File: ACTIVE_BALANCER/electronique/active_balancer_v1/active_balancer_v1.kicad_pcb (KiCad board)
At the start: 2 copper layers, 1 part, among them U1 LTC3300ILXE-2_PBF

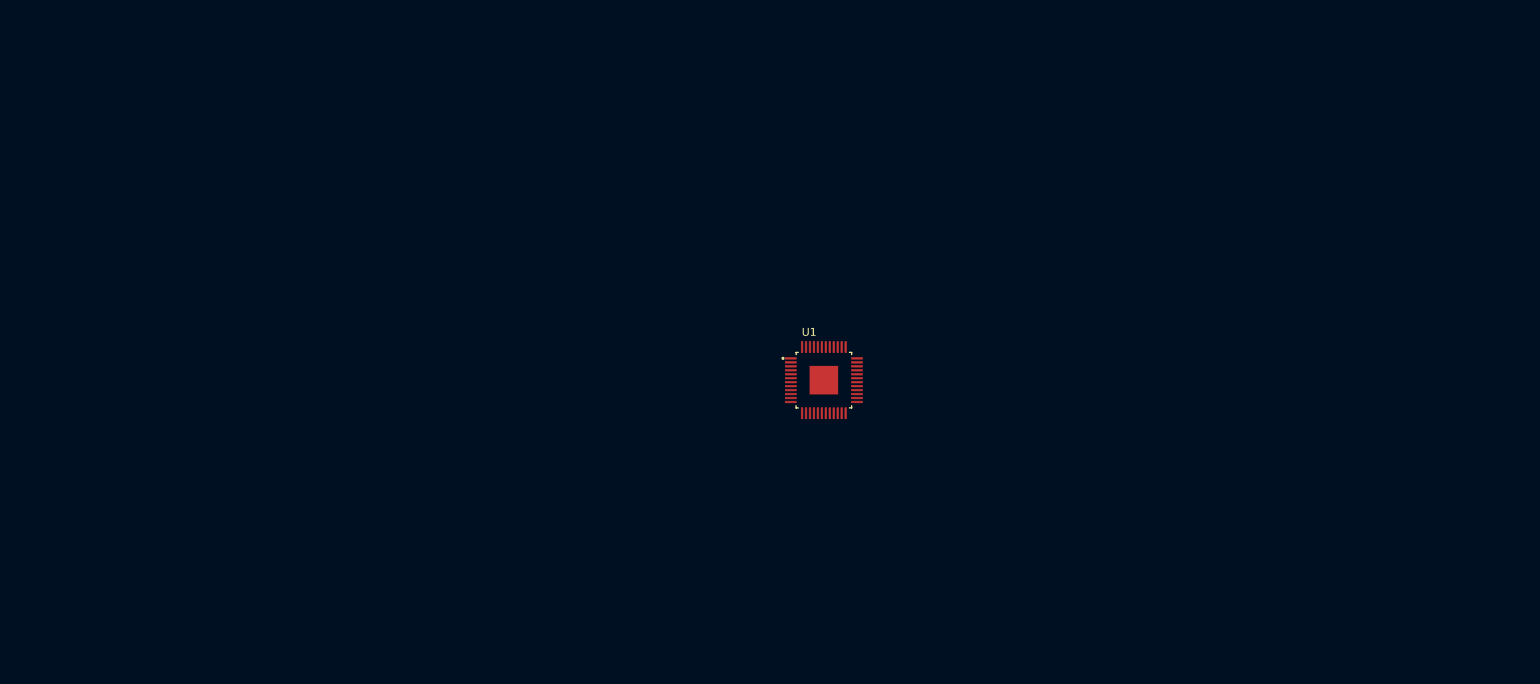
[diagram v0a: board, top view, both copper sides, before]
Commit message: finished the schematic need a review to make shure everything is okay and after pcb placing & routing while be made. Note this active balancer is for 6s scallable easly for 64s
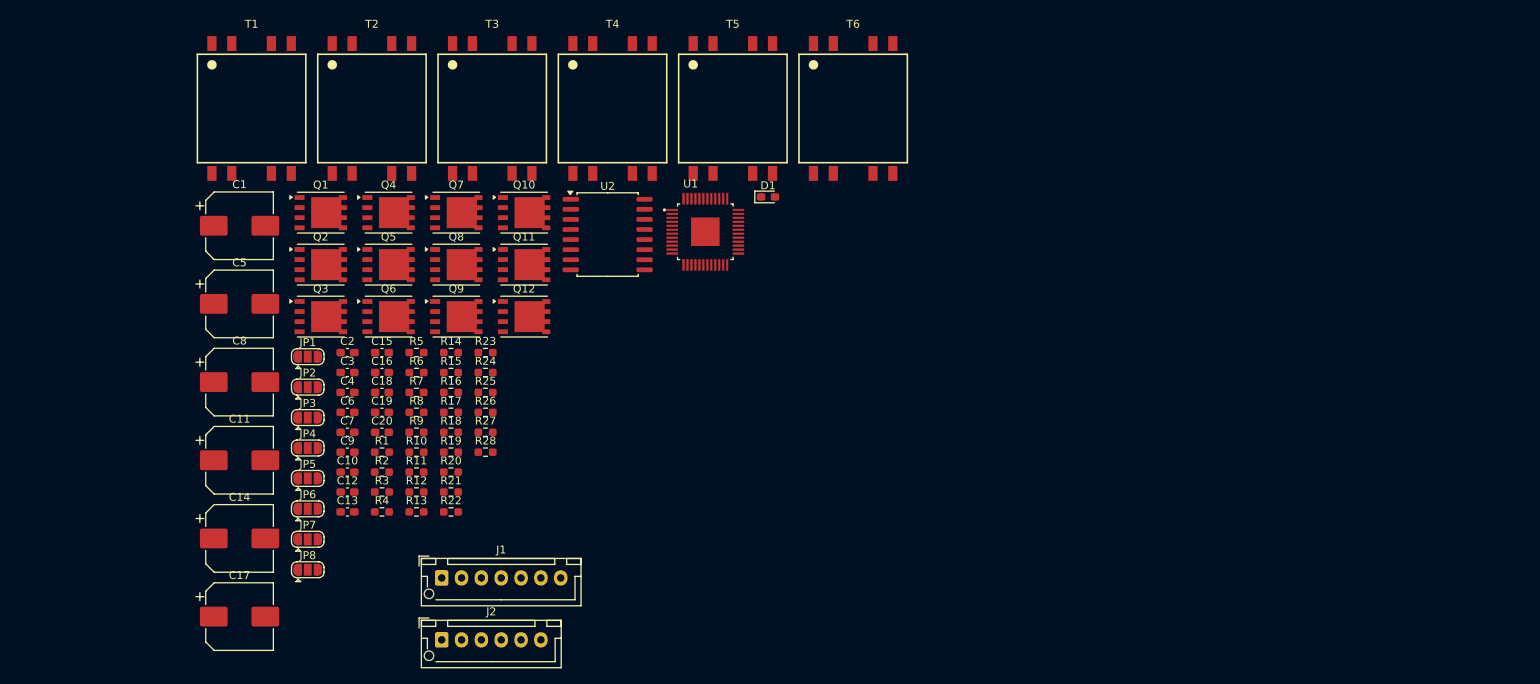
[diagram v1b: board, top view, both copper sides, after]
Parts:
- added C1: 60uF 10V, Capacitor_SMD:CP_Elec_8x10, F.Cu at (84.7, 70.7)
- added C10: 100pF 100V, Capacitor_SMD:C_0603_1608Metric_Pad1.08x0.95mm_HandSolder, F.Cu at (98.3, 101.7)
- added C11: 60uF 10V, Capacitor_SMD:CP_Elec_8x10, F.Cu at (84.7, 100.2)
- added C12: 100pF 100V, Capacitor_SMD:C_0603_1608Metric_Pad1.08x0.95mm_HandSolder, F.Cu at (98.3, 104.2)
- added C13: 100pF 100V, Capacitor_SMD:C_0603_1608Metric_Pad1.08x0.95mm_HandSolder, F.Cu at (98.3, 106.7)
- added C14: 60uF 10V, Capacitor_SMD:CP_Elec_8x10, F.Cu at (84.7, 110.1)
- added C15: 100pF 100V, Capacitor_SMD:C_0603_1608Metric_Pad1.08x0.95mm_HandSolder, F.Cu at (102.6, 86.6)
- added C16: 100pF 100V, Capacitor_SMD:C_0603_1608Metric_Pad1.08x0.95mm_HandSolder, F.Cu at (102.6, 89.1)
- added C17: 60uF 10V, Capacitor_SMD:CP_Elec_8x10, F.Cu at (84.7, 119.9)
- added C18: 100pF 100V, Capacitor_SMD:C_0603_1608Metric_Pad1.08x0.95mm_HandSolder, F.Cu at (102.6, 91.7)
- added C19: 100pF 100V, Capacitor_SMD:C_0603_1608Metric_Pad1.08x0.95mm_HandSolder, F.Cu at (102.6, 94.2)
- added C2: 100pF 100V, Capacitor_SMD:C_0603_1608Metric_Pad1.08x0.95mm_HandSolder, F.Cu at (98.3, 86.6)
- added C20: 0.1uF 10V, Capacitor_SMD:C_0603_1608Metric_Pad1.08x0.95mm_HandSolder, F.Cu at (102.6, 96.7)
- added C3: 100pF 100V, Capacitor_SMD:C_0603_1608Metric_Pad1.08x0.95mm_HandSolder, F.Cu at (98.3, 89.1)
- added C4: 10uF 10V, Capacitor_SMD:C_0603_1608Metric_Pad1.08x0.95mm_HandSolder, F.Cu at (98.3, 91.7)
- added C5: 60uF 10V, Capacitor_SMD:CP_Elec_8x10, F.Cu at (84.7, 80.5)
- added C6: 100pF 100V, Capacitor_SMD:C_0603_1608Metric_Pad1.08x0.95mm_HandSolder, F.Cu at (98.3, 94.2)
- added C7: 100pF 100V, Capacitor_SMD:C_0603_1608Metric_Pad1.08x0.95mm_HandSolder, F.Cu at (98.3, 96.7)
- added C8: 60uF 10V, Capacitor_SMD:CP_Elec_8x10, F.Cu at (84.7, 90.4)
- added C9: 100pF 100V, Capacitor_SMD:C_0603_1608Metric_Pad1.08x0.95mm_HandSolder, F.Cu at (98.3, 99.2)
- added D1: D_Schottky, Diode_SMD:D_0603_1608Metric_Pad1.05x0.95mm_HandSolder, F.Cu at (151.2, 67.0)
- added J1: JST_XH_6S, Connector_JST:JST_XH_B7B-XH-AM_1x07_P2.50mm_Vertical, F.Cu at (110.1, 115.0)
- added J2: JST_XH_6pin_SPI, Connector_JST:JST_XH_B6B-XH-AM_1x06_P2.50mm_Vertical, F.Cu at (110.1, 122.8)
- added JP1: JUMPER_A1, Jumper:SolderJumper-3_P1.3mm_Open_RoundedPad1.0x1.5mm, F.Cu at (93.3, 87.2)
- added JP2: JUMPER_A2, Jumper:SolderJumper-3_P1.3mm_Open_RoundedPad1.0x1.5mm, F.Cu at (93.3, 91.0)
- added JP3: JUMPER_A3, Jumper:SolderJumper-3_P1.3mm_Open_RoundedPad1.0x1.5mm, F.Cu at (93.3, 94.8)
- added JP4: JUMPER_A4, Jumper:SolderJumper-3_P1.3mm_Open_RoundedPad1.0x1.5mm, F.Cu at (93.3, 98.7)
- added JP5: JUMPER_A5, Jumper:SolderJumper-3_P1.3mm_Open_RoundedPad1.0x1.5mm, F.Cu at (93.3, 102.5)
- added JP6: JUMPER_EN_NUM_ISO_IN, Jumper:SolderJumper-3_P1.3mm_Open_RoundedPad1.0x1.5mm, F.Cu at (93.3, 106.3)
- added JP7: JUMPER_EN_NUM_ISO_OUT, Jumper:SolderJumper-3_P1.3mm_Open_RoundedPad1.0x1.5mm, F.Cu at (93.3, 110.2)
- added JP8: Whatchdog Timer, Jumper:SolderJumper-3_P1.3mm_Open_RoundedPad1.0x1.5mm, F.Cu at (93.3, 114.0)
- added Q1: SIR882DP 100V 60A, active_balancer:SIR882DP_PowerPAK_SO-8_Single, F.Cu at (94.9, 69.0)
- added Q10: SIR882DP 100V 60A, active_balancer:SIR882DP_PowerPAK_SO-8_Single, F.Cu at (120.5, 69.0)
- added Q11: SIR882DP 100V 60A, active_balancer:SIR882DP_PowerPAK_SO-8_Single, F.Cu at (120.5, 75.6)
- added Q12: SIR882DP 100V 60A, active_balancer:SIR882DP_PowerPAK_SO-8_Single, F.Cu at (120.5, 82.1)
- added Q2: SIR882DP 100V 60A, active_balancer:SIR882DP_PowerPAK_SO-8_Single, F.Cu at (94.9, 75.6)
- added Q3: SIR882DP 100V 60A, active_balancer:SIR882DP_PowerPAK_SO-8_Single, F.Cu at (94.9, 82.1)
- added Q4: SIR882DP 100V 60A, active_balancer:SIR882DP_PowerPAK_SO-8_Single, F.Cu at (103.4, 69.0)
- added Q5: SIR882DP 100V 60A, active_balancer:SIR882DP_PowerPAK_SO-8_Single, F.Cu at (103.4, 75.6)
- added Q6: SIR882DP 100V 60A, active_balancer:SIR882DP_PowerPAK_SO-8_Single, F.Cu at (103.4, 82.1)
- added Q7: SIR882DP 100V 60A, active_balancer:SIR882DP_PowerPAK_SO-8_Single, F.Cu at (112.0, 69.0)
- added Q8: SIR882DP 100V 60A, active_balancer:SIR882DP_PowerPAK_SO-8_Single, F.Cu at (112.0, 75.6)
- added Q9: SIR882DP 100V 60A, active_balancer:SIR882DP_PowerPAK_SO-8_Single, F.Cu at (112.0, 82.1)
- added R1: 10m, Resistor_SMD:R_0603_1608Metric_Pad0.98x0.95mm_HandSolder, F.Cu at (102.6, 99.2)
- added R10: 10m, Resistor_SMD:R_0603_1608Metric_Pad0.98x0.95mm_HandSolder, F.Cu at (107.0, 99.2)
- added R11: 330, Resistor_SMD:R_0603_1608Metric_Pad0.98x0.95mm_HandSolder, F.Cu at (107.0, 101.7)
- added R12: 10m, Resistor_SMD:R_0603_1608Metric_Pad0.98x0.95mm_HandSolder, F.Cu at (107.0, 104.2)
- added R13: 330, Resistor_SMD:R_0603_1608Metric_Pad0.98x0.95mm_HandSolder, F.Cu at (107.0, 106.7)
- added R14: 10m, Resistor_SMD:R_0603_1608Metric_Pad0.98x0.95mm_HandSolder, F.Cu at (111.3, 86.6)
- added R15: 330, Resistor_SMD:R_0603_1608Metric_Pad0.98x0.95mm_HandSolder, F.Cu at (111.3, 89.1)
- added R16: 10m, Resistor_SMD:R_0603_1608Metric_Pad0.98x0.95mm_HandSolder, F.Cu at (111.3, 91.7)
- added R17: 330, Resistor_SMD:R_0603_1608Metric_Pad0.98x0.95mm_HandSolder, F.Cu at (111.3, 94.2)
- added R18: 10m, Resistor_SMD:R_0603_1608Metric_Pad0.98x0.95mm_HandSolder, F.Cu at (111.3, 96.7)
- added R19: 330, Resistor_SMD:R_0603_1608Metric_Pad0.98x0.95mm_HandSolder, F.Cu at (111.3, 99.2)
- added R2: 10m, Resistor_SMD:R_0603_1608Metric_Pad0.98x0.95mm_HandSolder, F.Cu at (102.6, 101.7)
- added R20: 10m, Resistor_SMD:R_0603_1608Metric_Pad0.98x0.95mm_HandSolder, F.Cu at (111.3, 101.7)
- added R21: 330, Resistor_SMD:R_0603_1608Metric_Pad0.98x0.95mm_HandSolder, F.Cu at (111.3, 104.2)
- added R22: 10m, Resistor_SMD:R_0603_1608Metric_Pad0.98x0.95mm_HandSolder, F.Cu at (111.3, 106.7)
- added R23: 330, Resistor_SMD:R_0603_1608Metric_Pad0.98x0.95mm_HandSolder, F.Cu at (115.7, 86.6)
- added R24: 10m, Resistor_SMD:R_0603_1608Metric_Pad0.98x0.95mm_HandSolder, F.Cu at (115.7, 89.1)
- added R25: 330, Resistor_SMD:R_0603_1608Metric_Pad0.98x0.95mm_HandSolder, F.Cu at (115.7, 91.7)
- added R26: 10m, Resistor_SMD:R_0603_1608Metric_Pad0.98x0.95mm_HandSolder, F.Cu at (115.7, 94.2)
- added R27: 6.5, Resistor_SMD:R_0603_1608Metric_Pad0.98x0.95mm_HandSolder, F.Cu at (115.7, 96.7)
- added R28: 2.5k, Resistor_SMD:R_0603_1608Metric_Pad0.98x0.95mm_HandSolder, F.Cu at (115.7, 99.2)
- added R3: 330, Resistor_SMD:R_0603_1608Metric_Pad0.98x0.95mm_HandSolder, F.Cu at (102.6, 104.2)
- added R4: 330, Resistor_SMD:R_0603_1608Metric_Pad0.98x0.95mm_HandSolder, F.Cu at (102.6, 106.7)
- added R5: 23.33k, Resistor_SMD:R_0603_1608Metric_Pad0.98x0.95mm_HandSolder, F.Cu at (107.0, 86.6)
- added R6: 7.5k, Resistor_SMD:R_0603_1608Metric_Pad0.98x0.95mm_HandSolder, F.Cu at (107.0, 89.1)
- added R7: 330, Resistor_SMD:R_0603_1608Metric_Pad0.98x0.95mm_HandSolder, F.Cu at (107.0, 91.7)
- added R8: 10m, Resistor_SMD:R_0603_1608Metric_Pad0.98x0.95mm_HandSolder, F.Cu at (107.0, 94.2)
- added R9: 330, Resistor_SMD:R_0603_1608Metric_Pad0.98x0.95mm_HandSolder, F.Cu at (107.0, 96.7)
- added T1: 750312504 1:2 ISAT=10A 3.5uF, active_balancer:WE-FLYLT_EP13_2381, F.Cu at (86.2, 55.9)
- added T2: 750312504 1:2 ISAT=10A 3.5uF, active_balancer:WE-FLYLT_EP13_2381, F.Cu at (101.3, 55.9)
- added T3: 750312504 1:2 ISAT=10A 3.5uF, active_balancer:WE-FLYLT_EP13_2381, F.Cu at (116.5, 55.9)
- added T4: 750312504 1:2 ISAT=10A 3.5uF, active_balancer:WE-FLYLT_EP13_2381, F.Cu at (131.7, 55.9)
- added T5: 750312504 1:2 ISAT=10A 3.5uF, active_balancer:WE-FLYLT_EP13_2381, F.Cu at (146.8, 55.9)
- added T6: 750312504 1:2 ISAT=10A 3.5uF, active_balancer:WE-FLYLT_EP13_2381, F.Cu at (162.0, 55.9)
- added U2: ADuM1401xRW, Package_SO:SOIC-16W_7.5x10.3mm_P1.27mm, F.Cu at (131.0, 71.8)
- moved U1 23.9 mm to (143.4, 71.4)
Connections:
- U1 pad 1: unconnected-(U1-G6S-Pad1) -> /LT3300_G6S
- U1 pad 10: unconnected-(U1-I2S-Pad10) -> /LT3300_I2S
- U1 pad 11: unconnected-(U1-G1S-Pad11) -> /LT3300_G1S
- U1 pad 12: unconnected-(U1-I1S-Pad12) -> /LT3300_I1S
- U1 pad 13: unconnected-(U1-RTONS-Pad13) -> /LT3300_RTONS
- U1 pad 14: unconnected-(U1-RTONP-Pad14) -> /LT3300_RTONP
- U1 pad 15: unconnected-(U1-CTRL-Pad15) -> /CELL_1-
- U1 pad 16: unconnected-(U1-~{CSBI}-Pad16) -> /LT3300_CSBI
- U1 pad 17: unconnected-(U1-SCKI-Pad17) -> /LT3300_SCKI
- U1 pad 18: unconnected-(U1-SDI-Pad18) -> LT3300_SDI
- U1 pad 19: unconnected-(U1-SDO-Pad19) -> LT3300_SDO
- U1 pad 2: unconnected-(U1-I6S-Pad2) -> /LT3300_I6S
- U1 pad 20: unconnected-(U1-WDT-Pad20) -> /LT3300_WDT
- U1 pad 21: Net-(U1-V--Pad21) -> /CELL_1-
- U1 pad 22: unconnected-(U1-I1P-Pad22) -> /LT3300_I1P
- U1 pad 23: unconnected-(U1-G1P-Pad23) -> /LT3300_G1P
- U1 pad 24: unconnected-(U1-C1-Pad24) -> /CELL_1+
- U1 pad 25: unconnected-(U1-I2P-Pad25) -> /LT3300_I2P
- U1 pad 26: unconnected-(U1-G2P-Pad26) -> /LT3300_G2P
- U1 pad 27: unconnected-(U1-C2-Pad27) -> /CELL_2+
- U1 pad 28: unconnected-(U1-I3P-Pad28) -> /LT3300_I3P
- U1 pad 29: unconnected-(U1-G3P-Pad29) -> /LT3300_G3P
- U1 pad 3: unconnected-(U1-G5S-Pad3) -> /LT3300_G5S
- U1 pad 30: unconnected-(U1-C3-Pad30) -> /CELL_3+
- U1 pad 31: unconnected-(U1-I4P-Pad31) -> /LT3300_I4P
- U1 pad 32: unconnected-(U1-G4P-Pad32) -> /LT3300_G4P
- U1 pad 33: unconnected-(U1-C4-Pad33) -> /CELL_4+
- U1 pad 34: unconnected-(U1-I5P-Pad34) -> /LT3300_I5P
- U1 pad 35: unconnected-(U1-G5P-Pad35) -> /LT3300_G5P
- U1 pad 36: unconnected-(U1-C5-Pad36) -> /CELL_5+
- U1 pad 37: unconnected-(U1-I6P-Pad37) -> /LT3300_I6P
- U1 pad 38: unconnected-(U1-G6P-Pad38) -> /LT3300_G6P
- U1 pad 39: unconnected-(U1-C6-Pad39) -> /CELL_6+
- U1 pad 4: unconnected-(U1-I5S-Pad4) -> /LT3300_I5S
- U1 pad 40: unconnected-(U1-BOOSTP-Pad40) -> /LT3300_BOOSTP
- U1 pad 41: unconnected-(U1-BOOSTN-Pad41) -> /LT3300_BOOSTN
- U1 pad 42: unconnected-(U1-BOOST-Pad42) -> /LT3300_BOOST
- U1 pad 43: unconnected-(U1-A0-Pad43) -> /LT3300_A0
- U1 pad 44: unconnected-(U1-A1-Pad44) -> /LT3300_A1
- U1 pad 45: unconnected-(U1-A2-Pad45) -> /LT3300_A2
- U1 pad 46: unconnected-(U1-A3-Pad46) -> /LT3300_A3
- U1 pad 47: unconnected-(U1-A4-Pad47) -> /LT3300_A4
- U1 pad 48: unconnected-(U1-VREG-Pad48) -> /LT3300_BOOST
- U1 pad 49: Net-(U1-V--Pad21) -> /CELL_1-
- U1 pad 5: unconnected-(U1-G4S-Pad5) -> /LT3300_G4S
- U1 pad 6: unconnected-(U1-I4S-Pad6) -> /LT3300_I4S
- U1 pad 7: unconnected-(U1-G3S-Pad7) -> /LT3300_G3S
- U1 pad 8: unconnected-(U1-I3S-Pad8) -> /LT3300_I3S
- U1 pad 9: unconnected-(U1-G2S-Pad9) -> /LT3300_G2S

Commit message: Updated the pcb rooting and created a step file to check the finting in fusion 360
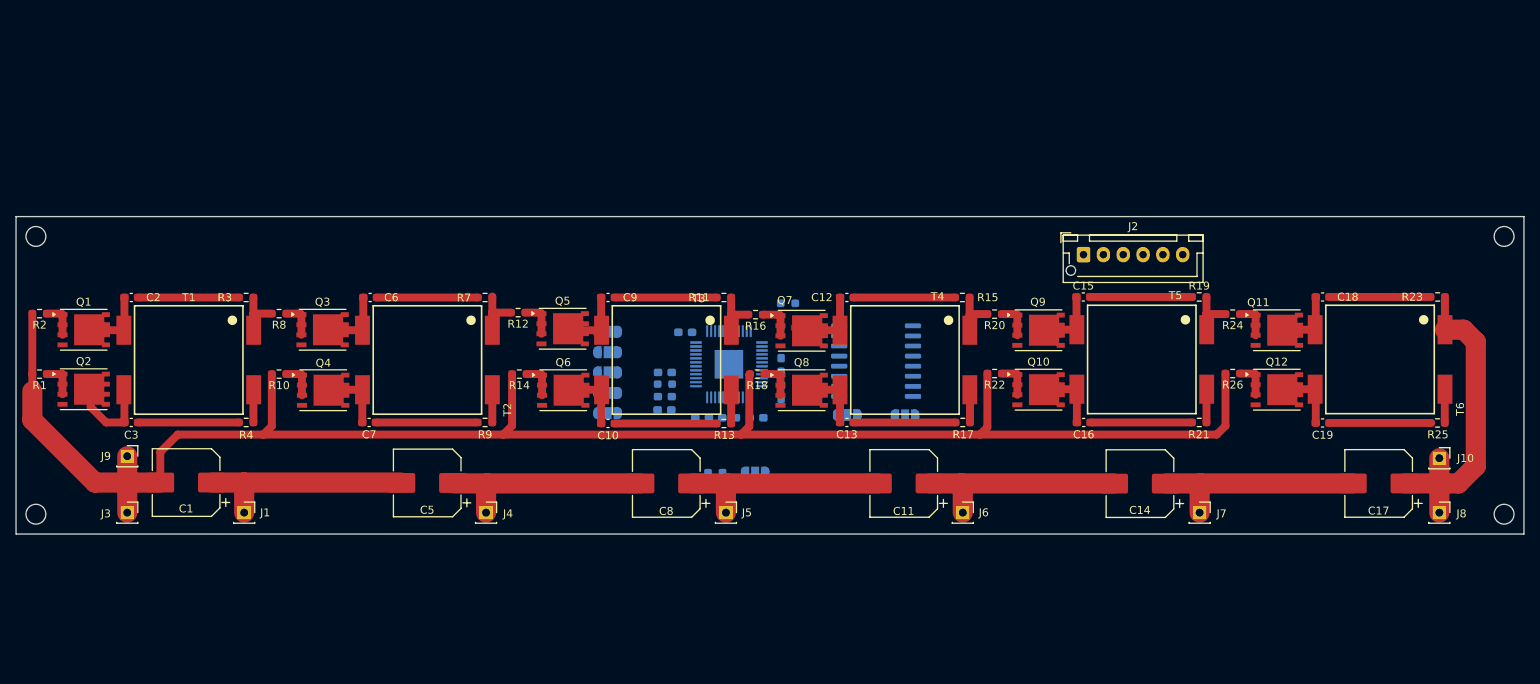
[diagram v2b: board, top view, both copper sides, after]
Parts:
- added C21: 0.1uF 10V, Capacitor_SMD:C_0603_1608Metric_Pad1.08x0.95mm_HandSolder, B.Cu at (138.2, 93.9)
- added C22: 0.1uF 10V, Capacitor_SMD:C_0603_1608Metric_Pad1.08x0.95mm_HandSolder, B.Cu at (142.9, 94.9)
- added C23: 0.1uF 10V, Capacitor_SMD:C_0603_1608Metric_Pad1.08x0.95mm_HandSolder, B.Cu at (146.3, 94.9)
- added C24: 0.1uF 10V, Capacitor_SMD:C_0603_1608Metric_Pad1.08x0.95mm_HandSolder, B.Cu at (149.8, 94.9)
- added C25: 0.1uF 10V, Capacitor_SMD:C_0603_1608Metric_Pad1.08x0.95mm_HandSolder, B.Cu at (152.9, 91.6)
- added C26: 0.1uF 10V, Capacitor_SMD:C_0603_1608Metric_Pad1.08x0.95mm_HandSolder, B.Cu at (152.9, 88.2)
- added J10: Conn_01x01_Socket, Connector_PinSocket_2.54mm:PinSocket_1x01_P2.54mm_Vertical, F.Cu at (235.8, 99.9)
- added J3: Conn_01x01_Socket, Connector_PinSocket_2.54mm:PinSocket_1x01_P2.54mm_Vertical, F.Cu at (70.5, 106.8)
- added J4: Conn_01x01_Socket, Connector_PinSocket_2.54mm:PinSocket_1x01_P2.54mm_Vertical, F.Cu at (115.7, 106.8)
- added J5: Conn_01x01_Socket, Connector_PinSocket_2.54mm:PinSocket_1x01_P2.54mm_Vertical, F.Cu at (145.9, 106.8)
- added J6: Conn_01x01_Socket, Connector_PinSocket_2.54mm:PinSocket_1x01_P2.54mm_Vertical, F.Cu at (175.8, 106.8)
- added J7: Conn_01x01_Socket, Connector_PinSocket_2.54mm:PinSocket_1x01_P2.54mm_Vertical, F.Cu at (205.6, 106.8)
- added J8: Conn_01x01_Socket, Connector_PinSocket_2.54mm:PinSocket_1x01_P2.54mm_Vertical, F.Cu at (235.8, 106.8)
- added J9: Conn_01x01_Socket, Connector_PinSocket_2.54mm:PinSocket_1x01_P2.54mm_Vertical, F.Cu at (70.5, 99.7)
- C20, C4, D1, JP1, JP2, JP3, JP4, JP5, JP6, JP7, JP8, R27, R28, R5, R6, U1, U2: moved to B.Cu
- J1: value JST_XH_6S -> Conn_01x01_Socket; footprint Connector_JST:JST_XH_B7B-XH-AM_1x07_P2.50mm_Vertical -> Connector_PinSocket_2.54mm:PinSocket_1x01_P2.54mm_Vertical
- moved C17 144.5 mm to (228.2, 103.1), turned to 180 degrees
- moved R23 120.2 mm to (235.6, 79.6), turned to 180 degrees
- moved R25 120.0 mm to (235.6, 95.5), turned to 180 degrees
- moved C18 119.1 mm to (221.1, 79.6), turned to 180 degrees
- moved C19 118.5 mm to (221.1, 95.5), turned to 180 degrees
- moved C14 113.7 mm to (198.1, 103.1), turned to 180 degrees
- moved R19 96.3 mm to (205.6, 79.6), turned to 180 degrees
- moved Q12 95.3 mm to (215.4, 91.3)
- moved Q11 95.2 mm to (215.4, 83.8)
- moved R21 94.7 mm to (205.6, 95.4), turned to 180 degrees
- moved R24 94.4 mm to (209.8, 81.8), turned to 180 degrees
- moved J2 94.3 mm to (191.0, 74.3)
- moved R26 94.3 mm to (209.8, 89.3), turned to 180 degrees
- moved C15 88.7 mm to (191.0, 79.6), turned to 180 degrees
- moved C16 88.7 mm to (191.0, 95.4), turned to 180 degrees
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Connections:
- net LT3300_CS renamed GLOBAL_LT3300_CS
- net LT3300_SCK renamed GLOBAL_LT3300_SCK
- J1 pad 1: /CELL_6+ -> /CELL_1+
- J2 pad 2: LT3300_SDO -> GLOBAL_LT3300_SDO
- J2 pad 3: LT3300_SDI -> GLOBAL_LT3300_SDI
- U1 pad 18: LT3300_SDI -> /LT3300_SDI
- U1 pad 19: LT3300_SDO -> /LT3300_SDO
- U2 pad 11: LT3300_SDO -> /LT3300_SDO
- U2 pad 12: LT3300_SDI -> /LT3300_SDI
- U2 pad 5: LT3300_SDI -> GLOBAL_LT3300_SDI
- U2 pad 6: LT3300_SDO -> GLOBAL_LT3300_SDO
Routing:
- net /CELL_1-: track 0.00 -> 218.2 mm
- net /CELL_6+: track 0.00 -> 41.1 mm
- net /CELL_1+: track 0.00 -> 34.1 mm
- net /CELL_2+: track 0.00 -> 33.9 mm
- net /CELL_5+: track 0.00 -> 33.8 mm
- net /CELL_3+: track 0.00 -> 33.4 mm
- net /CELL_4+: track 0.00 -> 33.4 mm
- net Net-(C15-Pad1): track 0.00 -> 12.8 mm
- net Net-(C13-Pad1): track 0.00 -> 12.8 mm
- net Net-(C9-Pad1): track 0.00 -> 12.8 mm
- net Net-(C19-Pad1): track 0.00 -> 12.8 mm
- net Net-(C10-Pad1): track 0.00 -> 12.8 mm
- net Net-(C16-Pad1): track 0.00 -> 12.8 mm
- net Net-(C12-Pad1): track 0.00 -> 12.8 mm
- net Net-(C18-Pad1): track 0.00 -> 12.7 mm
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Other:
- board outline added: 190 x 40 mm
